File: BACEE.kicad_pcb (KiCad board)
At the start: 2 copper layers, 17 parts, among them J1 Serial Port, J2 Digital pins, J3 I2C, J4 ISCP, U1 24LC1025, U2 DS1337S+, U3 24LC1025, U4 ATMEGA328-AU, Y1 Crystal 32KHz, Y2 Crystal 16MHz

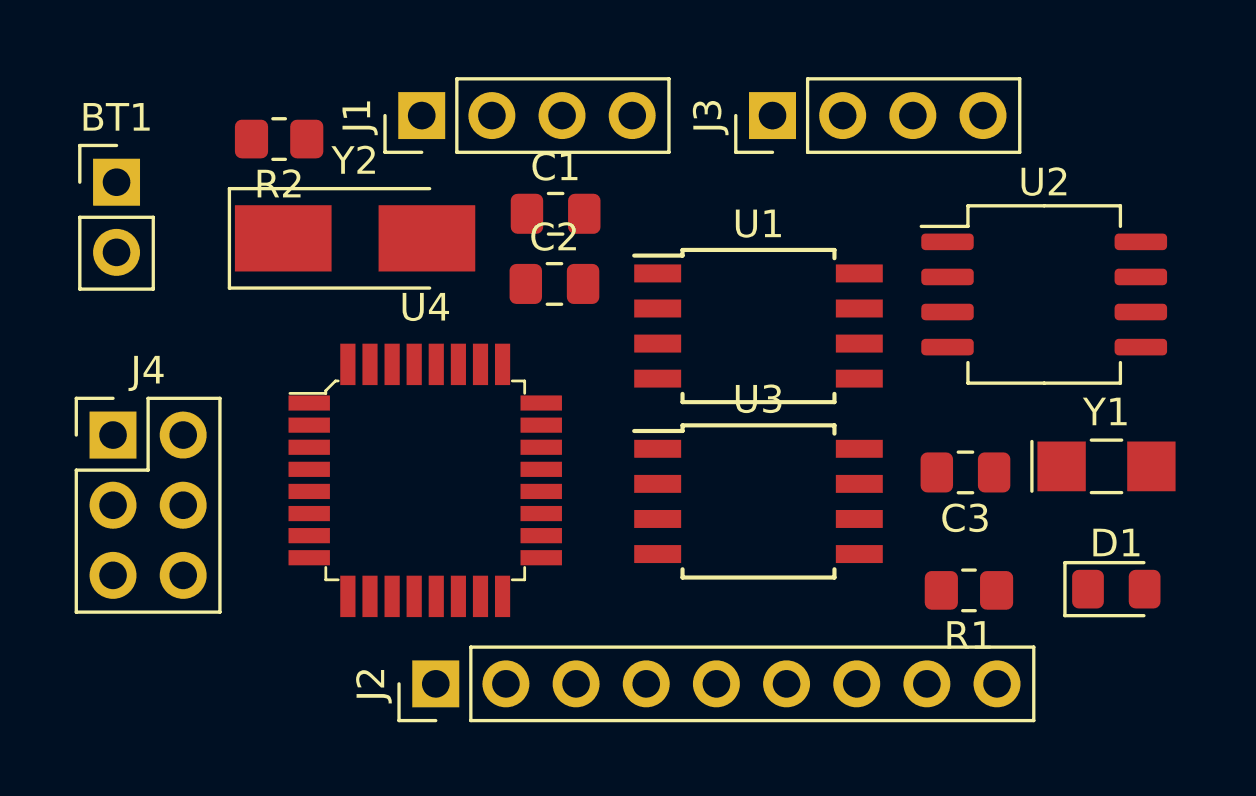
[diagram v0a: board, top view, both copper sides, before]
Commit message: Changed pin headers to pin sockets where necessary.
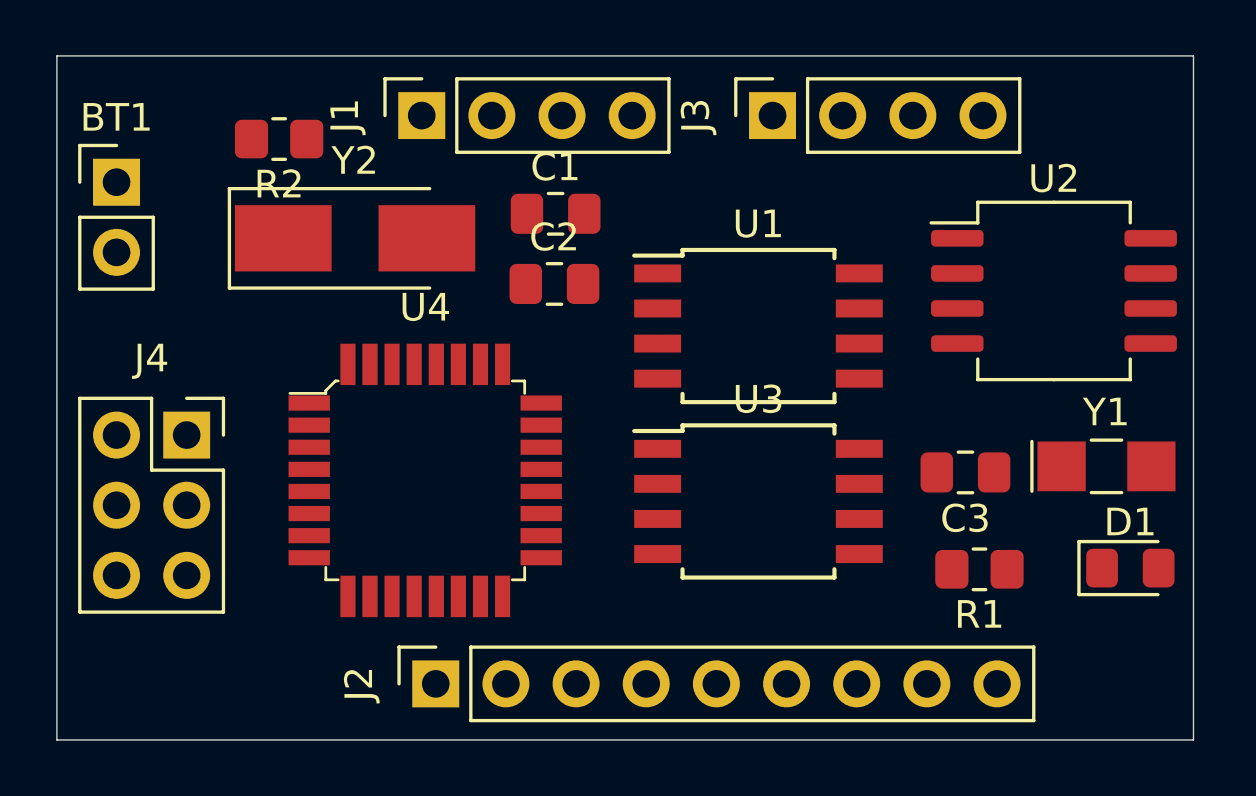
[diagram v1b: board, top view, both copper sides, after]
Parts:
- J1, J3: footprint Connector_PinHeader_2.54mm:PinHeader_1x04_P2.54mm_Vertical -> Connector_PinSocket_2.54mm:PinSocket_1x04_P2.54mm_Vertical
- J2: footprint Connector_PinHeader_2.54mm:PinHeader_1x09_P2.54mm_Vertical -> Connector_PinSocket_2.54mm:PinSocket_1x09_P2.54mm_Vertical
- J4: footprint Connector_PinHeader_2.54mm:PinHeader_2x03_P2.54mm_Vertical -> Connector_PinSocket_2.54mm:PinSocket_2x03_P2.54mm_Vertical
- moved J4 2.67 mm to (71.5, 108.1)
- moved D1 0.92 mm to (105.7, 112.9)
- moved R1 0.85 mm to (100.2, 112.9)
- moved U2 0.38 mm to (102.9, 102.9)
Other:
- board outline added: 41.1 x 24.8 mm

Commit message: Resized component designators.
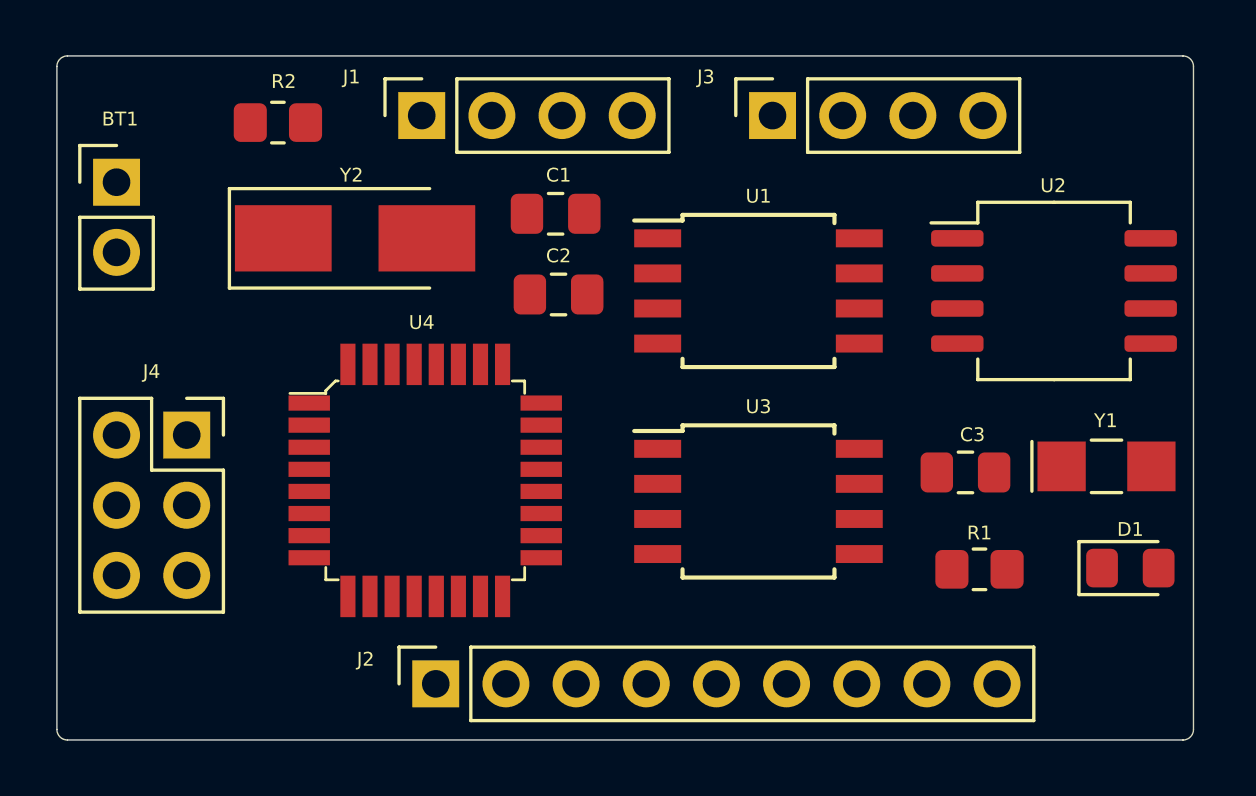
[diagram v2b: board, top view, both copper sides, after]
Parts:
- moved U1 1.27 mm to (92.2, 102.9)
- moved R2 0.60 mm to (74.8, 96.8)
- moved C2 0.41 mm to (85.0, 103.0)
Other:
- outline, holes or cut-outs redrawn
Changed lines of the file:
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@@
   (general
     (thickness 1.6)
-    (drawings 4)
+    (drawings 8)
     (tracks 0)
     (zones 0)
@@
     (descr "Through hole straight pin header, 1x02, 2.54mm pitch, single row")
     (tags "Through hole pin header THT 1x02 2.54mm single row")
-    (fp_text reference BT1 (at 0 -2.33) (layer F.SilkS)
-      (effects (font (size 1 1) (thickness 0.15)))
+    (fp_text reference BT1 (at 0.127 -2.286) (layer F.SilkS)
+      (effects (font (size 0.5 0.5) (thickness 0.125)))
     )
     (fp_text value "Battery 3V" (at 0 4.87) (layer F.Fab)
@@
     (tags "capacitor handsolder")
     (attr smd)
-    (fp_text reference C1 (at 0 -1.68) (layer F.SilkS)
-      (effects (font (size 1 1) (thickness 0.15)))
+    (fp_text reference C1 (at 0.1055 -1.397) (layer F.SilkS)
+      (effects (font (size 0.5 0.5) (thickness 0.125)))
     )
     (fp_text value "22 pF" (at 0 1.68) (layer F.Fab)
@@
   )
   (module Capacitor_SMD:C_0805_2012Metric_Pad1.18x1.45mm_HandSolder (layer F.Cu)
-    (at 84.8145 102.616)
+    (at 84.963 102.997)
     (descr "Capacitor SMD 0805 (2012 Metric), square (rectangular) end terminal, IPC_7351 nominal with elongated pad for handsoldering. (Body size source: IPC-SM-782 page 76, https://www.pcb-3d.com/wordpress/wp-content/uploads/ipc-sm-782a_amendment_1_and_2.pdf, https://docs.google.com/spreadsheets/d/1BsfQQcO9C6DZCsRaXUlFlo91Tg2WpOkGARC1WS5S8t0/edit?usp=sharing), generated with kicad-footprint-generator")
     (tags "capacitor handsolder")
     (attr smd)
-    (fp_text reference C2 (at 0 -1.68) (layer F.SilkS)
-      (effects (font (size 1 1) (thickness 0.15)))
+    (fp_text reference C2 (at 0 -1.397) (layer F.SilkS)
+      (effects (font (size 0.5 0.5) (thickness 0.125)))
     )
     (fp_text value "22 pF" (at 0 1.68) (layer F.Fab)
@@
     (tags "capacitor handsolder")
     (attr smd)
-    (fp_text reference C3 (at 0 -1.68) (layer F.SilkS)
-      (effects (font (size 1 1) (thickness 0.15)))
+    (fp_text reference C3 (at -0.254 1.363) (layer F.SilkS)
+      (effects (font (size 0.5 0.5) (thickness 0.125)))
     )
     (fp_text value "10 μF" (at 0 1.68) (layer F.Fab)
@@
     (tags "LED handsolder")
     (attr smd)
-    (fp_text reference D1 (at 0 -1.65) (layer F.SilkS)
-      (effects (font (size 1 1) (thickness 0.15)))
+    (fp_text reference D1 (at 0 -1.397) (layer F.SilkS)
+      (effects (font (size 0.5 0.5) (thickness 0.125)))
     )
     (fp_text value LED (at 0 1.65) (layer F.Fab)
@@
     (tags "resistor handsolder")
     (attr smd)
-    (fp_text reference R1 (at 0 -1.65) (layer F.SilkS)
-      (effects (font (size 1 1) (thickness 0.15)))
+    (fp_text reference R1 (at 0 1.315) (layer F.SilkS)
+      (effects (font (size 0.5 0.5) (thickness 0.125)))
     )
     (fp_text value "330 Ω" (at 0 1.65) (layer F.Fab)
@@
   )
   (module Resistor_SMD:R_0805_2012Metric_Pad1.20x1.40mm_HandSolder (layer F.Cu)
-    (at 74.847 97.37 180)
+    (at 74.803 96.774 180)
     (descr "Resistor SMD 0805 (2012 Metric), square (rectangular) end terminal, IPC_7351 nominal with elongated pad for handsoldering. (Body size source: IPC-SM-782 page 72, https://www.pcb-3d.com/wordpress/wp-content/uploads/ipc-sm-782a_amendment_1_and_2.pdf), generated with kicad-footprint-generator")
     (tags "resistor handsolder")
     (attr smd)
-    (fp_text reference R2 (at 0 -1.65) (layer F.SilkS)
-      (effects (font (size 1 1) (thickness 0.15)))
+    (fp_text reference R2 (at -0.21 1.485) (layer F.SilkS)
+      (effects (font (size 0.5 0.5) (thickness 0.125)))
     )
     (fp_text value "10K Ω" (at 0 1.65) (layer F.Fab)
@@
   )
   (module Package_SO:SOIJ-8_5.3x5.3mm_P1.27mm (layer F.Cu)
-    (at 92.202 104.14)
+    (at 92.202 102.87)
     (descr "8-Lead Plastic Small Outline (SM) - Medium, 5.28 mm Body [SOIC] (see Microchip Packaging Specification 00000049BS.pdf)")
     (tags "SOIC 1.27")
     (attr smd)
-    (fp_text reference U1 (at 0 -3.68) (layer F.SilkS)
-      (effects (font (size 1 1) (thickness 0.15)))
+    (fp_text reference U1 (at 0 -3.429) (layer F.SilkS)
+      (effects (font (size 0.5 0.5) (thickness 0.125)))
     )
     (fp_text value 24LC1025 (at 0 3.68) (layer F.Fab)
@@
     (tags "SO SO")
     (attr smd)
-    (fp_text reference U2 (at 0 -4.05) (layer F.SilkS)
-      (effects (font (size 1 1) (thickness 0.15)))
+    (fp_text reference U2 (at -0.031 -3.81) (layer F.SilkS)
+      (effects (font (size 0.5 0.5) (thickness 0.125)))
     )
     (fp_text value DS1337S+ (at 0 4.05) (layer F.Fab)
@@
     (tags "SOIC 1.27")
     (attr smd)
-    (fp_text reference U3 (at 0 -3.68) (layer F.SilkS)
-      (effects (font (size 1 1) (thickness 0.15)))
+    (fp_text reference U3 (at 0 -3.429) (layer F.SilkS)
+      (effects (font (size 0.5 0.5) (thickness 0.125)))
     )
     (fp_text value 24LC1025 (at 0 3.68) (layer F.Fab)
@@
     (descr http://www.atmel.com/Images/Atmel-8826-SEEPROM-PCB-Mounting-Guidelines-Surface-Mount-Packages-ApplicationNote.pdf)
     (attr smd)
-    (fp_text reference U4 (at 0 -6.25) (layer F.SilkS)
-      (effects (font (size 1 1) (thickness 0.15)))
+    (fp_text reference U4 (at -0.127 -5.715) (layer F.SilkS)
+      (effects (font (size 0.5 0.5) (thickness 0.125)))
     )
     (fp_text value ATMEGA328-AU (at 0 6.2) (layer F.Fab)
@@
     (tags "SMD SMT crystal hand-soldering")
     (attr smd)
-    (fp_text reference Y1 (at 0 -1.95) (layer F.SilkS)
-      (effects (font (size 1 1) (thickness 0.15)))
+    (fp_text reference Y1 (at -0.026 -1.651) (layer F.SilkS)
+      (effects (font (size 0.5 0.5) (thickness 0.125)))
     )
     (fp_text value "Crystal 32KHz" (at 0 1.95) (layer F.Fab)
@@
     (tags "SMD SMT crystal hand-soldering")
     (attr smd)
-    (fp_text reference Y2 (at 0 -2.8) (layer F.SilkS)
-      (effects (font (size 1 1) (thickness 0.15)))
+    (fp_text reference Y2 (at -0.127 -2.286) (layer F.SilkS)
+      (effects (font (size 0.5 0.5) (thickness 0.125)))
     )
     (fp_text value "Crystal 16MHz" (at 0 2.8) (layer F.Fab)
@@
     (descr "Through hole straight socket strip, 1x04, 2.54mm pitch, single row (from Kicad 4.0.7), script generated")
     (tags "Through hole socket strip THT 1x04 2.54mm single row")
-    (fp_text reference J1 (at 0 -2.77 90) (layer F.SilkS)
-      (effects (font (size 1 1) (thickness 0.15)))
+    (fp_text reference J1 (at 1.397 -2.54 180) (layer F.SilkS)
+      (effects (font (size 0.5 0.5) (thickness 0.125)))
     )
     (fp_text value "Serial Port" (at 0 10.39 90) (layer F.Fab)
@@
     (descr "Through hole straight socket strip, 1x09, 2.54mm pitch, single row (from Kicad 4.0.7), script generated")
     (tags "Through hole socket strip THT 1x09 2.54mm single row")
-    (fp_text reference J2 (at 0 -2.77 90) (layer F.SilkS)
-      (effects (font (size 1 1) (thickness 0.15)))
+    (fp_text reference J2 (at 0.889 -2.54 180) (layer F.SilkS)
+      (effects (font (size 0.5 0.5) (thickness 0.125)))
     )
     (fp_text value "Digital pins" (at 0 23.09 90) (layer F.Fab)
@@
     (descr "Through hole straight socket strip, 1x04, 2.54mm pitch, single row (from Kicad 4.0.7), script generated")
     (tags "Through hole socket strip THT 1x04 2.54mm single row")
-    (fp_text reference J3 (at 0 -2.77 90) (layer F.SilkS)
-      (effects (font (size 1 1) (thickness 0.15)))
+    (fp_text reference J3 (at 1.397 -2.413 180) (layer F.SilkS)
+      (effects (font (size 0.5 0.5) (thickness 0.125)))
     )
     (fp_text value I2C (at 0 10.39 90) (layer F.Fab)
@@
     (descr "Through hole straight socket strip, 2x03, 2.54mm pitch, double cols (from Kicad 4.0.7), script generated")
     (tags "Through hole socket strip THT 2x03 2.54mm double row")
-    (fp_text reference J4 (at -1.27 -2.77) (layer F.SilkS)
-      (effects (font (size 1 1) (thickness 0.15)))
+    (fp_text reference J4 (at -1.27 -2.296) (layer F.SilkS)
+      (effects (font (size 0.5 0.5) (thickness 0.125)))
     )
     (fp_text value ISCP (at -1.27 7.85) (layer F.Fab)
@@
     )
   )
-  (gr_line (start 107.95 119.126) (end 107.95 94.361) (layer Edge.Cuts) (width 0.05))
-  (gr_line (start 66.802 119.126) (end 107.95 119.126) (layer Edge.Cuts) (width 0.05))
-  (gr_line (start 66.802 94.361) (end 66.802 119.126) (layer Edge.Cuts) (width 0.05))
-  (gr_line (start 107.95 94.361) (end 66.802 94.361) (layer Edge.Cuts) (width 0.05))
+  (gr_line (start 66.802 94.742) (end 66.802 118.745) (layer Edge.Cuts) (width 0.05))
+  (gr_line (start 107.569 94.361) (end 67.183 94.361) (layer Edge.Cuts) (width 0.05))
+  (gr_line (start 107.95 118.745) (end 107.95 94.742) (layer Edge.Cuts) (width 0.05))
+  (gr_line (start 67.183 119.126) (end 107.569 119.126) (layer Edge.Cuts) (width 0.05))
+  (gr_arc (start 107.569 94.742) (end 107.95 94.742) (angle -90) (layer Edge.Cuts) (width 0.05))
+  (gr_arc (start 107.569 118.745) (end 107.569 119.126) (angle -90) (layer Edge.Cuts) (width 0.05))
+  (gr_arc (start 67.183 118.745) (end 66.802 118.745) (angle -90) (layer Edge.Cuts) (width 0.05))
+  (gr_arc (start 67.183 94.742) (end 67.183 94.361) (angle -90) (layer Edge.Cuts) (width 0.05))
 )

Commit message: Added outline and mounting holes
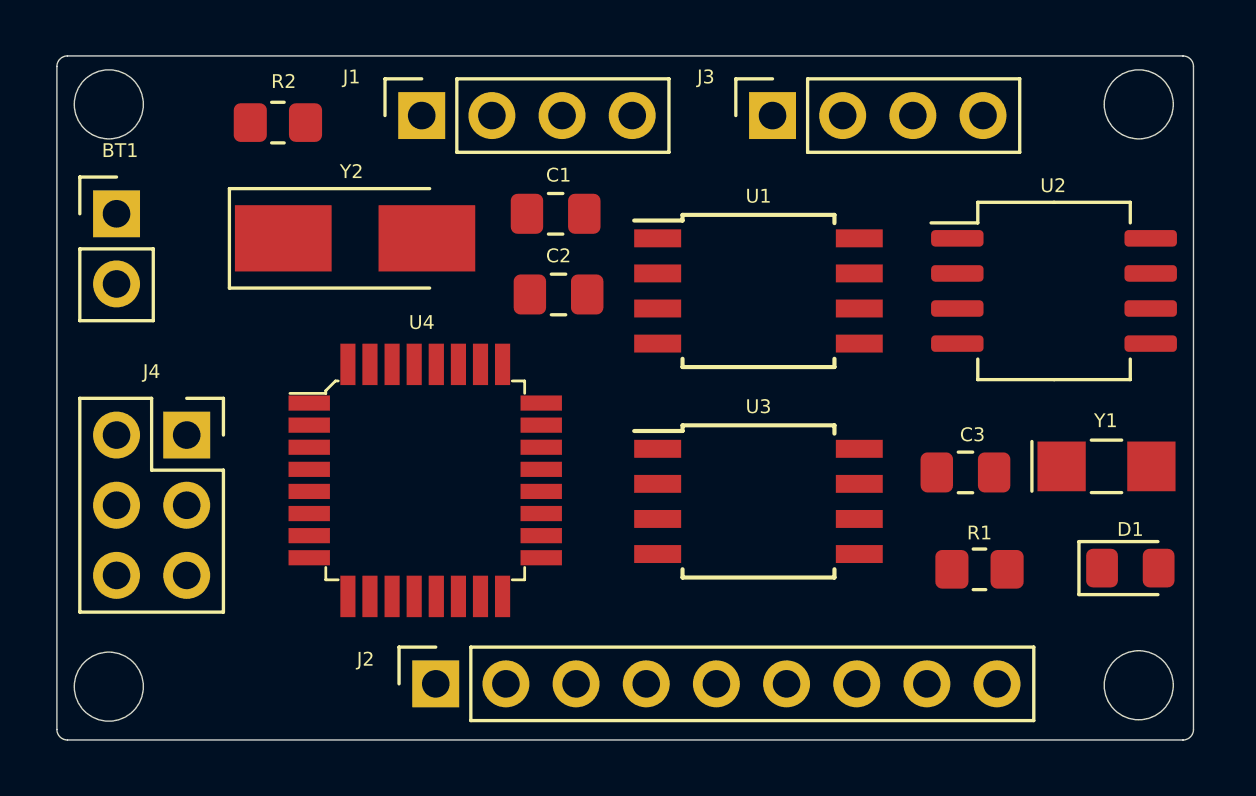
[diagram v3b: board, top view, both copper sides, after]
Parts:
- moved BT1 1.14 mm to (69.0, 100.1)
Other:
- outline, holes or cut-outs redrawn
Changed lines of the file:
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@@
   (general
     (thickness 1.6)
-    (drawings 8)
+    (drawings 12)
     (tracks 0)
     (zones 0)
@@
   )
   (module Connector_PinHeader_2.54mm:PinHeader_1x02_P2.54mm_Vertical (layer F.Cu)
-    (at 68.961 98.933)
+    (at 68.961 100.076)
     (descr "Through hole straight pin header, 1x02, 2.54mm pitch, single row")
     (tags "Through hole pin header THT 1x02 2.54mm single row")
@@
     (tags "SMD SMT crystal hand-soldering")
     (attr smd)
-    (fp_text reference Y2 (at -0.127 -2.286) (layer F.SilkS)
+    (fp_text reference Y2 (at -0.127 -2.413) (layer F.SilkS)
       (effects (font (size 0.5 0.5) (thickness 0.125)))
     )
@@
     )
   )
+  (gr_circle (center 105.9688 96.1136) (end 107.2188 96.1136) (layer Edge.Cuts) (width 0.05))
+  (gr_circle (center 105.9688 117.1448) (end 107.2188 117.1448) (layer Edge.Cuts) (width 0.05))
+  (gr_circle (center 68.6816 117.1956) (end 69.9316 117.1956) (layer Edge.Cuts) (width 0.05))
+  (gr_circle (center 68.6816 96.1136) (end 69.9316 96.1136) (layer Edge.Cuts) (width 0.05))
   (gr_line (start 66.802 94.742) (end 66.802 118.745) (layer Edge.Cuts) (width 0.05))
   (gr_line (start 107.569 94.361) (end 67.183 94.361) (layer Edge.Cuts) (width 0.05))

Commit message: Created copper filled area for board routed in 2 layers.
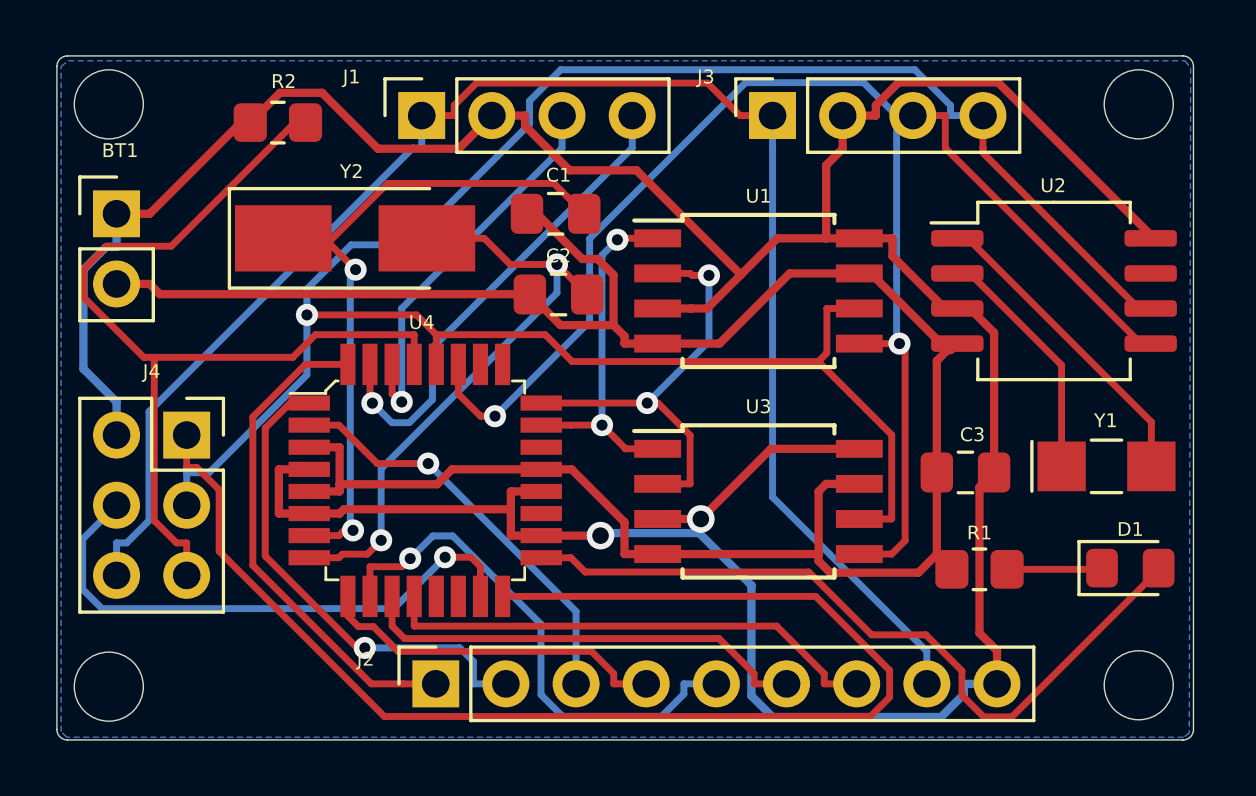
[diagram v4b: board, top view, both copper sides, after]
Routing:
- net /Vcc: track 0.00 -> 131.0 mm, vias 0 -> 2
- net /SCL: track 0.00 -> 80.5 mm, vias 0 -> 1
- net GNDPWR: track 0.00 -> 80.1 mm
- net /Connectors/GND: track 0.00 -> 58.4 mm
- net /SDA: track 0.00 -> 56.7 mm, vias 0 -> 2
- net /MISO: track 0.00 -> 48.0 mm
- net /RESET: track 0.00 -> 34.1 mm
- net Net-(D1-Pad2): track 0.00 -> 27.5 mm
- net Net-(C1-Pad2): track 0.00 -> 24.9 mm, vias 0 -> 2
- net Net-(C2-Pad2): track 0.00 -> 22.1 mm, vias 0 -> 2
- net /MOSI: track 0.00 -> 20.2 mm, vias 0 -> 1
- net /D6: track 0.00 -> 19.0 mm, vias 0 -> 1
- net /D8: track 0.00 -> 18.2 mm
- net /D2: track 0.00 -> 18.0 mm
- net /D3: track 0.00 -> 17.7 mm, vias 0 -> 1
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- added copper zone on B.Cu, net GNDPWR
